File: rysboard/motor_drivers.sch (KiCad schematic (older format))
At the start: 27 parts, among them J2 Motor L, J3 Motor R, U1 L6470, U2 L6470

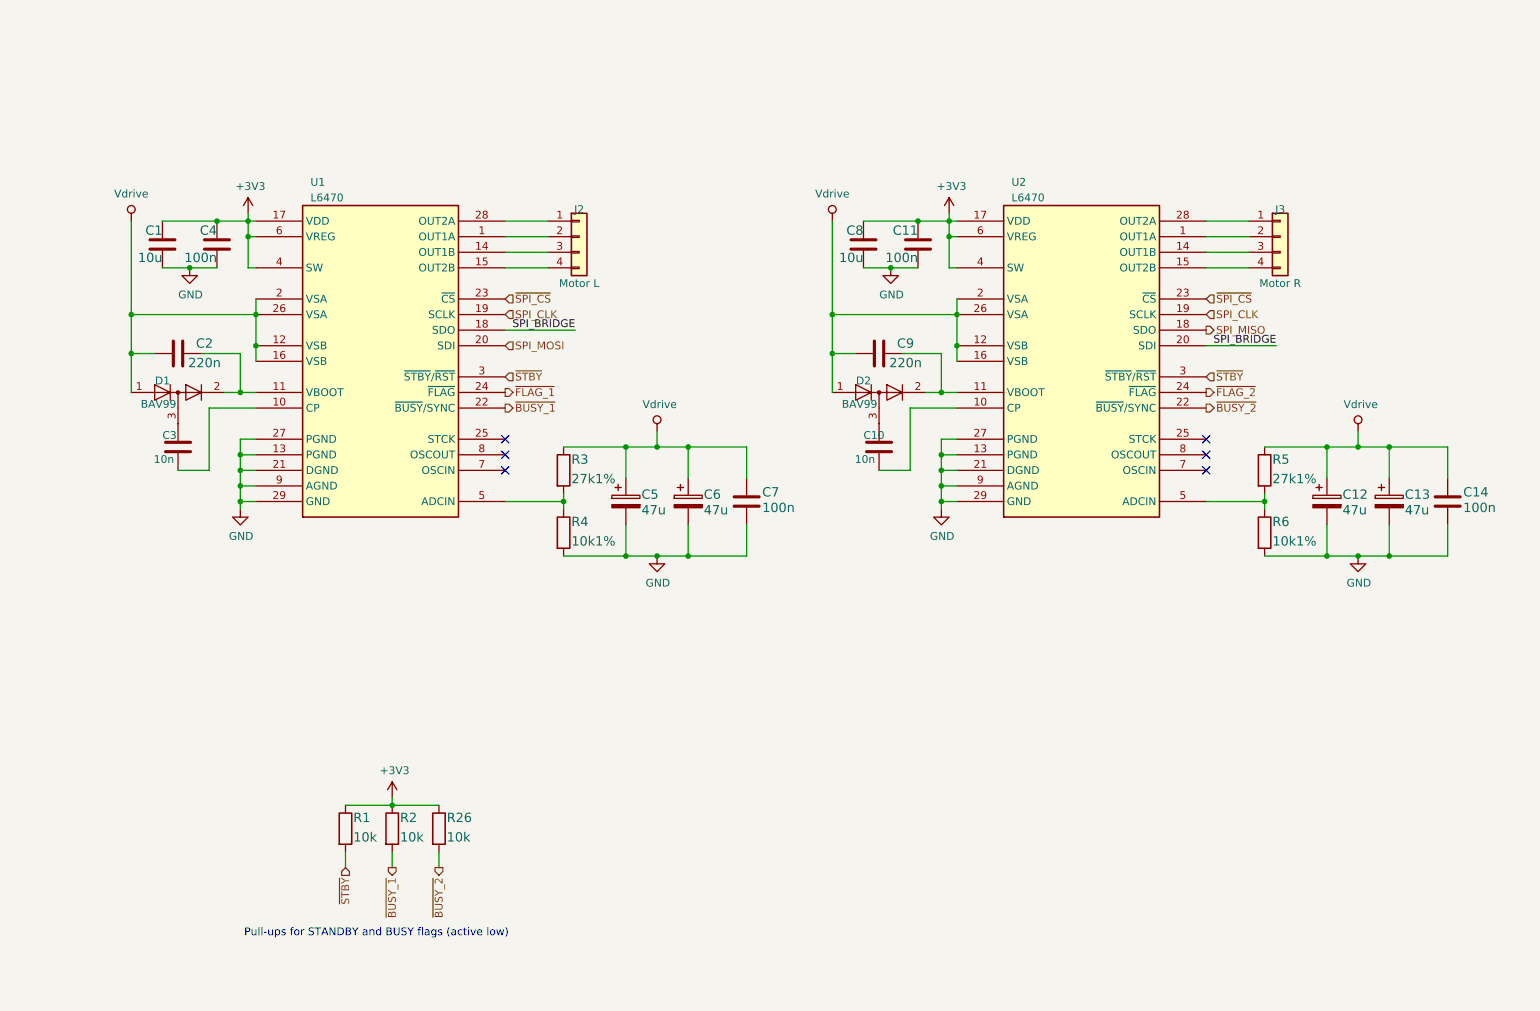
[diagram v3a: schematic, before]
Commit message: rysboard 4.2: * add converter output protection (shottky, D8) * fix converter resistor values (R13/R14) * add 5Vgood LED (D9) * add PWR_FLAGs for KiCAD's ERC * add NAND for motor driver's output flags * add pull-ups for motor driver's FLAG outputs
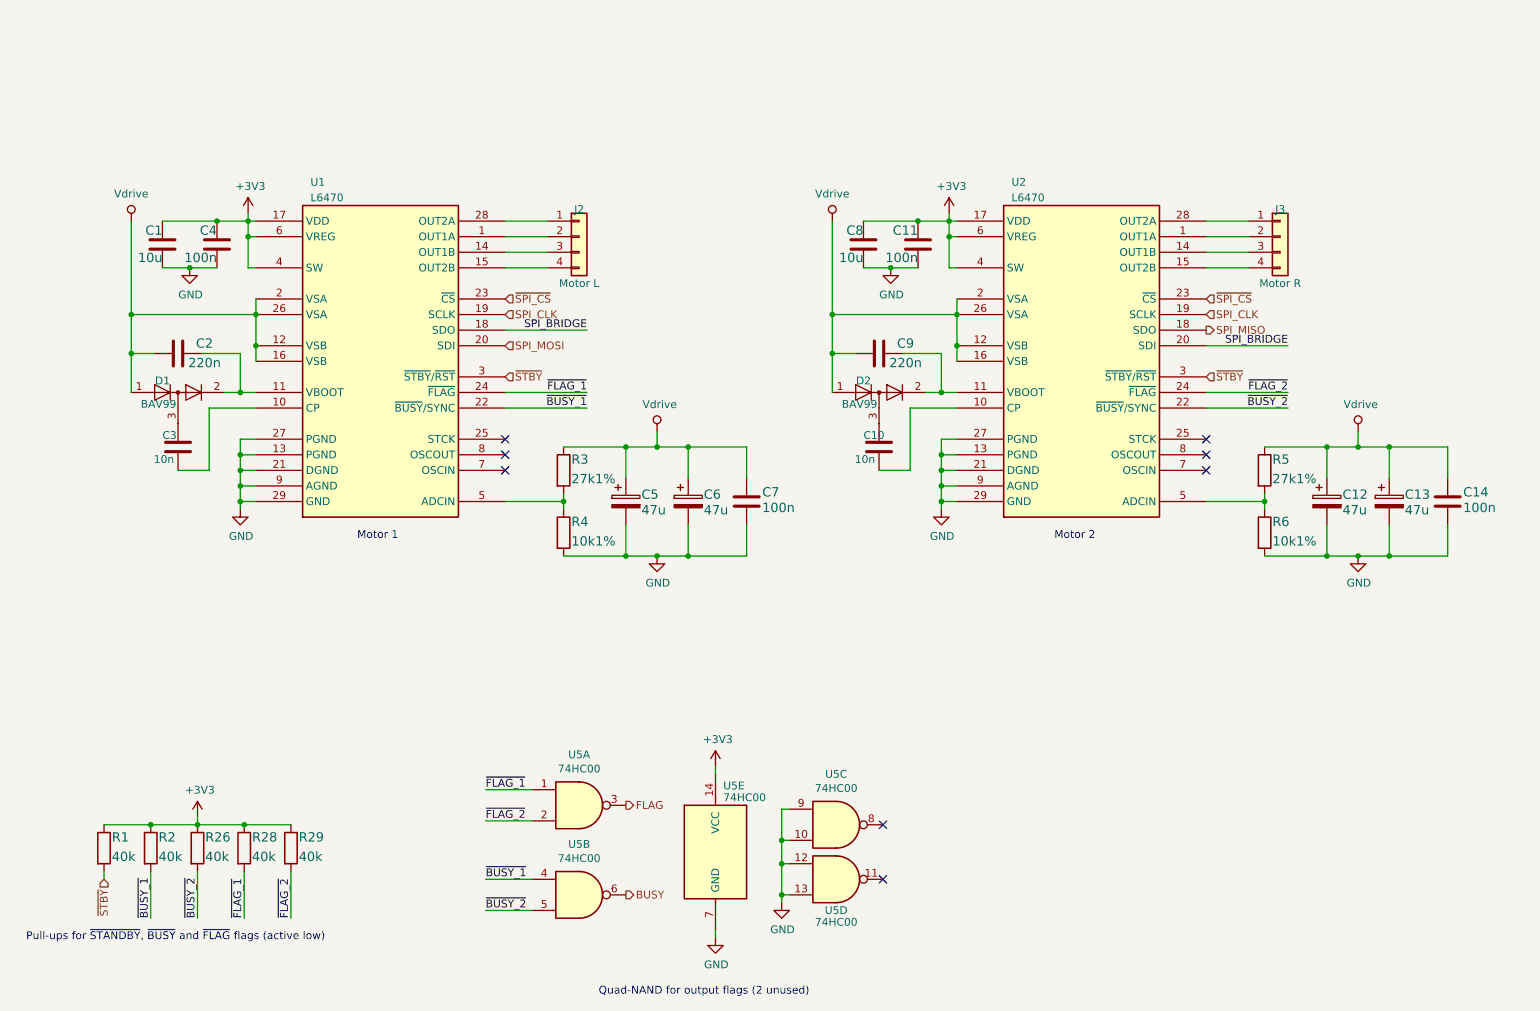
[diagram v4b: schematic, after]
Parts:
- added R28, R29: 40k, Resistor_SMD:R_0603_1608Metric, symbol Device:R
- added U5: 74HC00, symbol 74xx:74HC00
- R1, R2, R26: value 10k -> 40k
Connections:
- net +3V3: now also R28.1, R29.1, U5.14 (VCC)
- net GND: now also U5.10, U5.12, U5.13, U5.7 (GND), U5.9
- net ~BUSY_1: now also U5.4
- net ~BUSY_2: now also U5.5
- net ~FLAG_1: now also R28.2, U5.1
- net ~FLAG_2: now also R29.2, U5.2
- new net BUSY: U5.6
- new net FLAG: U5.3
- no-connect marks 6 -> 8
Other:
- note added: "Motor 1"
- note added: "Motor 2"
- note added: "Pull-ups for ~STANDBY~, ~BUSY~ and ~FLAG~ flags (active low)"
- note added: "Quad-NAND for output flags (2 unused)"
- note removed: "Pull-ups for STANDBY and BUSY flags (active low)"
- moved on the sheet: R1, R2, R26

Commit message: rysboard v4.2: * route the whole board (TODO: ground fills, track width checks) * fix half of ToF connectors missing ground connection * swap LEDs for easier routing
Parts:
- removed unit 3 of U5
- removed unit 4 of U5
- removed unit 5 of U5
- U5: value 74HC00 -> 74AHC2G00; footprint (none) -> Package_SO:TSSOP-8_3x3mm_P0.65mm; symbol 74xx:74HC00 -> 74xGxx:74AHC2G00
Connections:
- net +3V3: now also U5.8 (VCC), U5.8 (VCC)
- net BUSY: now also U5.3; no longer U5.6
- net FLAG: now also U5.7; no longer U5.3
- net GND: now also U5.4 (GND), U5.4 (GND)
- net ~BUSY_1: now also U5.5; no longer U5.4
- net ~BUSY_2: now also U5.6; no longer U5.5
- no-connect marks 8 -> 6
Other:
- note added: "Dual-NAND for output flags"
- note removed: "Quad-NAND for output flags (2 unused)"
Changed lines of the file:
@@
 Text Notes 7575 4150 0    50   ~ 0
 Motor 2
-$Comp
-L power:GND #PWR022
-U 1 1 5EDBA6E6
-P 5825 6475
-F 0 "#PWR022" H 5825 6225 50  0001 C CNN
-F 1 "GND" H 5830 6302 50  0000 C CNN
-F 2 "" H 5825 6475 50  0001 C CNN
-F 3 "" H 5825 6475 50  0001 C CNN
-	1    5825 6475
-	1    0    0    -1
-$EndComp
-Connection ~ 5825 6425
-Wire Wire Line
-	5825 6425 5825 6475
-Connection ~ 5825 6225
-Wire Wire Line
-	5825 6425 5875 6425
-Wire Wire Line
-	5825 6225 5825 6425
-Connection ~ 5825 6075
-Wire Wire Line
-	5825 6225 5875 6225
-Wire Wire Line
-	5825 6075 5825 6225
-Wire Wire Line
-	5825 6075 5875 6075
-Wire Wire Line
-	5825 5875 5825 6075
-Wire Wire Line
-	5875 5875 5825 5875
-Text Notes 4650 7075 0    50   ~ 0
-Quad-NAND for output flags (2 unused)
-Text Label 3925 5950 0    50   ~ 0
+Text Notes 4000 6875 0    50   ~ 0
+Dual-NAND for output flags
+Text Label 3925 5900 0    50   ~ 0
 ~FLAG_2
-Text Label 3925 6525 0    50   ~ 0
+Text Label 3925 6175 0    50   ~ 0
 ~BUSY_2
 Wire Wire Line
-	4225 6525 3925 6525
+	4225 6175 3925 6175
 Wire Wire Line
-	4225 5950 3925 5950
-Text Label 3925 5750 0    50   ~ 0
+	4225 5900 3925 5900
+Text Label 3925 5800 0    50   ~ 0
 ~FLAG_1
-Text Label 3925 6325 0    50   ~ 0
+Text Label 3925 6075 0    50   ~ 0
 ~BUSY_1
 Wire Wire Line
-	4225 6325 3925 6325
+	4225 6075 3925 6075
 Wire Wire Line
-	4225 5750 3925 5750
-NoConn ~ 6475 5975
-NoConn ~ 6475 6325
+	4225 5800 3925 5800
 Wire Wire Line
-	5400 6700 5400 6650
+	4525 6350 4525 6225
 $Comp
 L power:GND #PWR021
 U 1 1 5EC696A7
-P 5400 6700
-F 0 "#PWR021" H 5400 6450 50  0001 C CNN
-F 1 "GND" H 5405 6527 50  0000 C CNN
-F 2 "" H 5400 6700 50  0001 C CNN
-F 3 "" H 5400 6700 50  0001 C CNN
-	1    5400 6700
+P 4525 6350
+F 0 "#PWR021" H 4525 6100 50  0001 C CNN
+F 1 "GND" H 4530 6177 50  0000 C CNN
+F 2 "" H 4525 6350 50  0001 C CNN
+F 3 "" H 4525 6350 50  0001 C CNN
+	1    4525 6350
 	1    0    0    -1
 $EndComp
 Wire Wire Line
-	5400 5600 5400 5650
+	4525 5625 4525 5750
 $Comp
 L power:+3V3 #PWR019
 U 1 1 5EC5D3A7
-P 5400 5600
-F 0 "#PWR019" H 5400 5450 50  0001 C CNN
-F 1 "+3V3" H 5415 5773 50  0000 C CNN
-F 2 "" H 5400 5600 50  0001 C CNN
-F 3 "" H 5400 5600 50  0001 C CNN
-	1    5400 5600
+P 4525 5625
+F 0 "#PWR019" H 4525 5475 50  0001 C CNN
+F 1 "+3V3" H 4540 5798 50  0000 C CNN
+F 2 "" H 4525 5625 50  0001 C CNN
+F 3 "" H 4525 5625 50  0001 C CNN
+	1    4525 5625
 	1    0    0    -1
 $EndComp
 $Comp
-L 74xx:74HC00 U5
-U 5 1 5EC2B932
-P 5400 6150
-F 0 "U5" H 5450 6575 50  0000 L CNN
-F 1 "74HC00" H 5450 6500 50  0000 L CNN
-F 2 "" H 5400 6150 50  0001 C CNN
-F 3 "http://www.ti.com/lit/gpn/sn74hc00" H 5400 6150 50  0001 C CNN
-	5    5400 6150
+L 74xGxx:74AHC2G00 U5
+U 2 1 5EC23E03
+P 4525 6125
+F 0 "U5" H 4600 5975 50  0000 C CNN
+F 1 "74AHC2G00" H 4750 5900 50  0000 C CNN
+F 2 "Package_SO:TSSOP-8_3x3mm_P0.65mm" H 4525 6125 50  0001 C CNN
+F 3 "https://assets.nexperia.com/documents/data-sheet/74AHC_AHCT2G00.pdf" H 4525 6125 50  0001 C CNN
+	2    4525 6125
 	1    0    0    -1
 $EndComp
 $Comp
-L 74xx:74HC00 U5
-U 4 1 5EC295FB
-P 6175 6325
-F 0 "U5" H 6175 6125 50  0000 C CNN
-F 1 "74HC00" H 6175 6050 50  0000 C CNN
-F 2 "" H 6175 6325 50  0001 C CNN
-F 3 "http://www.ti.com/lit/gpn/sn74hc00" H 6175 6325 50  0001 C CNN
-	4    6175 6325
-	1    0    0    -1
-$EndComp
-$Comp
-L 74xx:74HC00 U5
-U 3 1 5EC27BBA
-P 6175 5975
-F 0 "U5" H 6175 6300 50  0000 C CNN
-F 1 "74HC00" H 6175 6209 50  0000 C CNN
-F 2 "" H 6175 5975 50  0001 C CNN
-F 3 "http://www.ti.com/lit/gpn/sn74hc00" H 6175 5975 50  0001 C CNN
-	3    6175 5975
-	1    0    0    -1
-$EndComp
-$Comp
-L 74xx:74HC00 U5
-U 2 1 5EC23E03
-P 4525 6425
-F 0 "U5" H 4525 6750 50  0000 C CNN
-F 1 "74HC00" H 4525 6659 50  0000 C CNN
-F 2 "" H 4525 6425 50  0001 C CNN
-F 3 "http://www.ti.com/lit/gpn/sn74hc00" H 4525 6425 50  0001 C CNN
-	2    4525 6425
-	1    0    0    -1
-$EndComp
-$Comp
-L 74xx:74HC00 U5
+L 74xGxx:74AHC2G00 U5
 U 1 1 5EC22288
 P 4525 5850
-F 0 "U5" H 4525 6175 50  0000 C CNN
-F 1 "74HC00" H 4525 6084 50  0000 C CNN
-F 2 "" H 4525 5850 50  0001 C CNN
-F 3 "http://www.ti.com/lit/gpn/sn74hc00" H 4525 5850 50  0001 C CNN
+F 0 "U5" H 4600 6075 50  0000 C CNN
+F 1 "74AHC2G00" H 4750 6000 50  0000 C CNN
+F 2 "Package_SO:TSSOP-8_3x3mm_P0.65mm" H 4525 5850 50  0001 C CNN
+F 3 "https://assets.nexperia.com/documents/data-sheet/74AHC_AHCT2G00.pdf" H 4525 5850 50  0001 C CNN
 	1    4525 5850
 	1    0    0    -1
 $EndComp
-Text HLabel 4825 6425 2    50   Output ~ 0
+Text HLabel 4775 6125 2    50   Output ~ 0
 BUSY
-Text HLabel 4825 5850 2    50   Output ~ 0
+Text HLabel 4775 5850 2    50   Output ~ 0
 FLAG
 $EndSCHEMATC

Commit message: rysboard: changed LED and sensors' VCC to 5V
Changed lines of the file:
@@
 Connection ~ 2350 3200
 Wire Wire Line
-	2350 3200 2450 3200
+	2350 3200 2425 3200
 Wire Wire Line
 	2450 3300 2150 3300
@@
 Connection ~ 6850 3200
 Wire Wire Line
-	6850 3200 6950 3200
+	6850 3200 6925 3200
 Wire Wire Line
 	6950 3300 6650 3300
@@
 Text HLabel 4775 5850 2    50   Output ~ 0
 FLAG
+$Comp
+L power:PWR_FLAG #FLG0105
+U 1 1 5ECC8EEC
+P 6925 3200
+F 0 "#FLG0105" H 6925 3275 50  0001 C CNN
+F 1 "PWR_FLAG" H 6925 3373 50  0000 C CNN
+F 2 "" H 6925 3200 50  0001 C CNN
+F 3 "~" H 6925 3200 50  0001 C CNN
+	1    6925 3200
+	1    0    0    -1
+$EndComp
+Connection ~ 6925 3200
+Wire Wire Line
+	6925 3200 6950 3200
+$Comp
+L power:PWR_FLAG #FLG0106
+U 1 1 5ECCA600
+P 2425 3200
+F 0 "#FLG0106" H 2425 3275 50  0001 C CNN
+F 1 "PWR_FLAG" H 2425 3373 50  0000 C CNN
+F 2 "" H 2425 3200 50  0001 C CNN
+F 3 "~" H 2425 3200 50  0001 C CNN
+	1    2425 3200
+	1    0    0    -1
+$EndComp
+Connection ~ 2425 3200
+Wire Wire Line
+	2425 3200 2450 3200
 $EndSCHEMATC

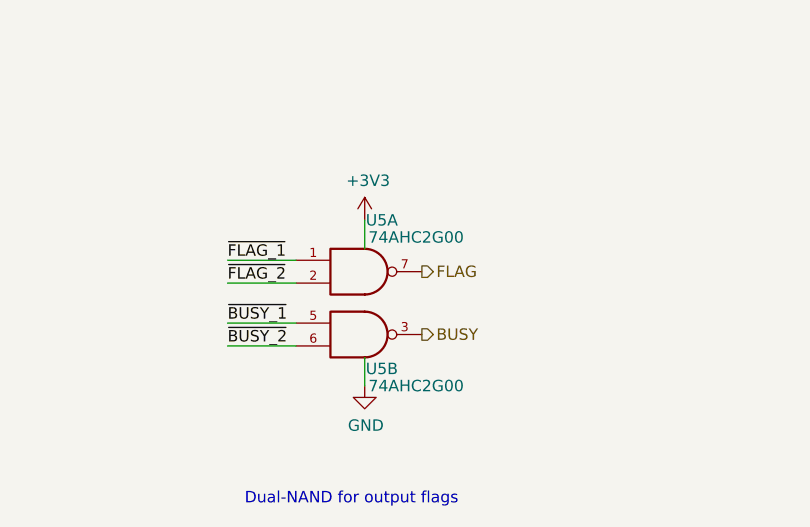
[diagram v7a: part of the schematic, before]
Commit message: rysboard: move D8 before converter feedback; replace U5 with counterpart of higher availability; fix U4 wiring; improve GND connections to motor drivers
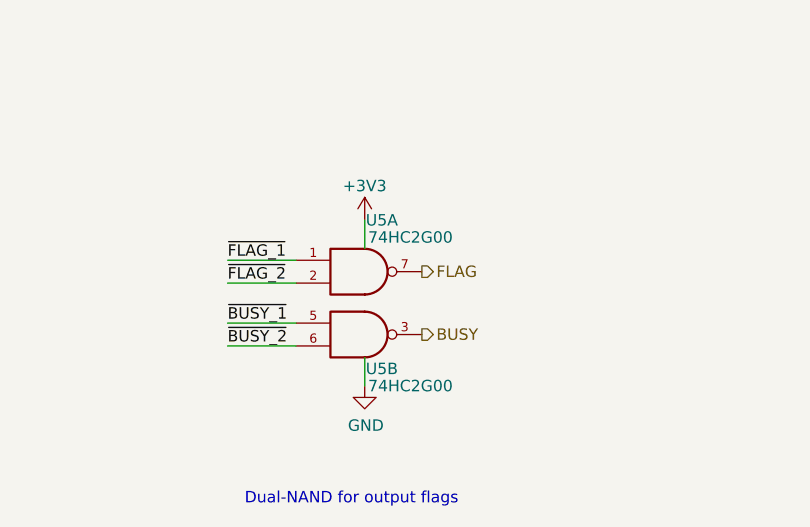
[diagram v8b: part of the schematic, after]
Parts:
- removed U5: 74AHC2G00, Package_SO:TSSOP-8_3x3mm_P0.65mm, symbol 74xGxx:74AHC2G00
- added U5: 74HC2G00, Package_SO:TSSOP-8_3x3mm_P0.65mm, symbol rysboard:74HC2G00
- U1, U2: PartID (none) -> L6470H; TME (none) -> https://www.tme.eu/pl/details/l6470h/drivery-silnikowe-i-pw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
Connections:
- net +3V3: now also U5.8 (VCC), U5.8 (VCC)
- net BUSY: now also U5.3
- net FLAG: now also U5.7
- net GND: now also U5.4 (GND), U5.4 (GND)
- net ~BUSY_1: now also U5.5
- net ~BUSY_2: now also U5.6
- net ~FLAG_1: now also U5.1
- net ~FLAG_2: now also U5.2
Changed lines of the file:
@@
 F 2 "Package_SO:HTSSOP-28-1EP_4.4x9.7mm_P0.65mm_EP3.4x9.5mm_ThermalVias" H 3250 2350 50  0001 C CNN
 F 3 "https://www.st.com/resource/en/datasheet/l6470.pdf" H 3250 3200 50  0001 C CNN
+F 4 "L6470H" H 3250 3200 50  0001 C CNN "PartID"
+F 5 "https://www.tme.eu/pl/details/l6470h/drivery-silnikowe-i-pwm/stmicroelectronics/" H 3250 3200 50  0001 C CNN "TME"
 	1    3250 3200
 	1    0    0    -1
@@
 F 2 "Package_SO:HTSSOP-28-1EP_4.4x9.7mm_P0.65mm_EP3.4x9.5mm_ThermalVias" H 7750 2350 50  0001 C CNN
 F 3 "https://www.st.com/resource/en/datasheet/l6470.pdf" H 7750 3200 50  0001 C CNN
+F 4 "L6470H" H 7750 3200 50  0001 C CNN "PartID"
+F 5 "https://www.tme.eu/pl/details/l6470h/drivery-silnikowe-i-pwm/stmicroelectronics/" H 7750 3200 50  0001 C CNN "TME"
 	1    7750 3200
 	1    0    0    -1
@@
 P 4525 5625
 F 0 "#PWR019" H 4525 5475 50  0001 C CNN
-F 1 "+3V3" H 4540 5798 50  0000 C CNN
+F 1 "+3V3" H 4525 5775 50  0000 C CNN
 F 2 "" H 4525 5625 50  0001 C CNN
 F 3 "" H 4525 5625 50  0001 C CNN
 	1    4525 5625
-	1    0    0    -1
-$EndComp
-$Comp
-L 74xGxx:74AHC2G00 U5
-U 2 1 5EC23E03
-P 4525 6125
-F 0 "U5" H 4600 5975 50  0000 C CNN
-F 1 "74AHC2G00" H 4750 5900 50  0000 C CNN
-F 2 "Package_SO:TSSOP-8_3x3mm_P0.65mm" H 4525 6125 50  0001 C CNN
-F 3 "https://assets.nexperia.com/documents/data-sheet/74AHC_AHCT2G00.pdf" H 4525 6125 50  0001 C CNN
-	2    4525 6125
-	1    0    0    -1
-$EndComp
-$Comp
-L 74xGxx:74AHC2G00 U5
-U 1 1 5EC22288
-P 4525 5850
-F 0 "U5" H 4600 6075 50  0000 C CNN
-F 1 "74AHC2G00" H 4750 6000 50  0000 C CNN
-F 2 "Package_SO:TSSOP-8_3x3mm_P0.65mm" H 4525 5850 50  0001 C CNN
-F 3 "https://assets.nexperia.com/documents/data-sheet/74AHC_AHCT2G00.pdf" H 4525 5850 50  0001 C CNN
-	1    4525 5850
 	1    0    0    -1
 $EndComp
@@
 Wire Wire Line
 	2425 3200 2450 3200
+$Comp
+L rysboard:74HC2G00 U5
+U 1 1 5FB5A7BC
+P 4525 5850
+F 0 "U5" H 4600 6075 50  0000 C CNN
+F 1 "74HC2G00" H 4725 6000 50  0000 C CNN
+F 2 "Package_SO:TSSOP-8_3x3mm_P0.65mm" H 4525 5850 50  0001 C CNN
+F 3 "https://assets.nexperia.com/documents/data-sheet/74HC_HCT2G00.pdf" H 4525 5850 50  0001 C CNN
+	1    4525 5850
+	1    0    0    -1
+$EndComp
+$Comp
+L rysboard:74HC2G00 U5
+U 2 1 5FB5B2B0
+P 4525 6125
+F 0 "U5" H 4600 5975 50  0000 C CNN
+F 1 "74HC2G00" H 4725 5900 50  0000 C CNN
+F 2 "Package_SO:TSSOP-8_3x3mm_P0.65mm" H 4525 6125 50  0001 C CNN
+F 3 "https://assets.nexperia.com/documents/data-sheet/74HC_HCT2G00.pdf" H 4525 6125 50  0001 C CNN
+F 4 " 74HC2G00DP.125" H 4525 6125 50  0001 C CNN "PartID"
+F 5 "https://www.tme.eu/pl/details/74hc2g00dp.125/bramki-inwertery/nexperia/" H 4525 6125 50  0001 C CNN "TME"
+	2    4525 6125
+	1    0    0    -1
+$EndComp
 $EndSCHEMATC
